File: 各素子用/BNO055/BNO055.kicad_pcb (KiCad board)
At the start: 2 copper layers, 17.2 x 17.1 mm, 25 parts, among them J2 Conn_01x04_Socket, U1 LP5907MFX-2.8, U2 BNO055, Y1 Crystal

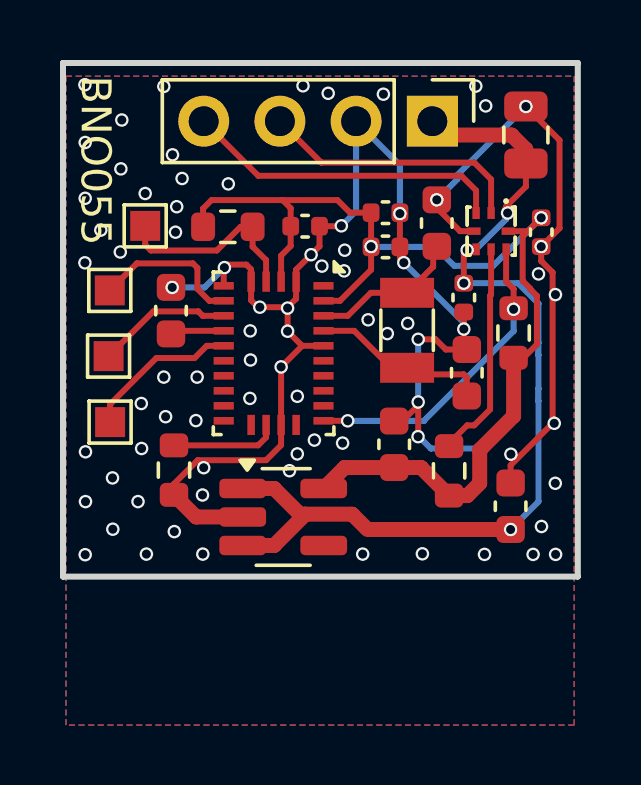
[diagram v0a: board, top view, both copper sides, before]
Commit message: RX-ESP delete
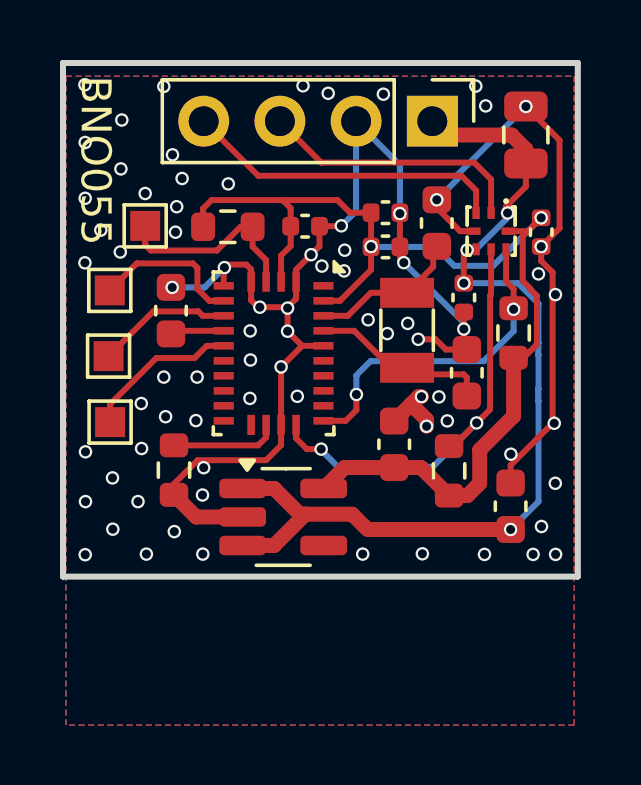
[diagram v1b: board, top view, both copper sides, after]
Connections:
- R2 pad 2: Net-(U3-B1) -> Net-(U2-COM1)
- U2 pad 19: unconnected-(U2-COM1-Pad19) -> Net-(U2-COM1)
- U3 pad 6: Net-(U3-B1) -> Net-(U2-COM1)
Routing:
- net Net-(U2-COM1): track 0.00 -> 14.7 mm, vias 0 -> 2
- net Net-(U3-B1): track 7.28 -> 0.00 mm
- net GND: track 64.9 -> 60.7 mm, vias 79 -> 77
- net Net-(U2-COM0): track 10.4 -> 11.1 mm
